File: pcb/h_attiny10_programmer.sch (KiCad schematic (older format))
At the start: 43 parts, among them J1 PWR, J2 AVR-TPI-6, J3 Conn_01x03, J4 Conn_01x03, J5 Conn_01x03, J6 Conn_01x03, J7 Conn_01x03, J8 Conn_01x03, Q1 2N3906, SW1 SW_Push, SW2 SW_Push, SW3 SW_Push, SW4 SW_Push, U1 AM1SS-n(j)z, U2 PC817, U3 L7805, U4 ATtiny10-TS

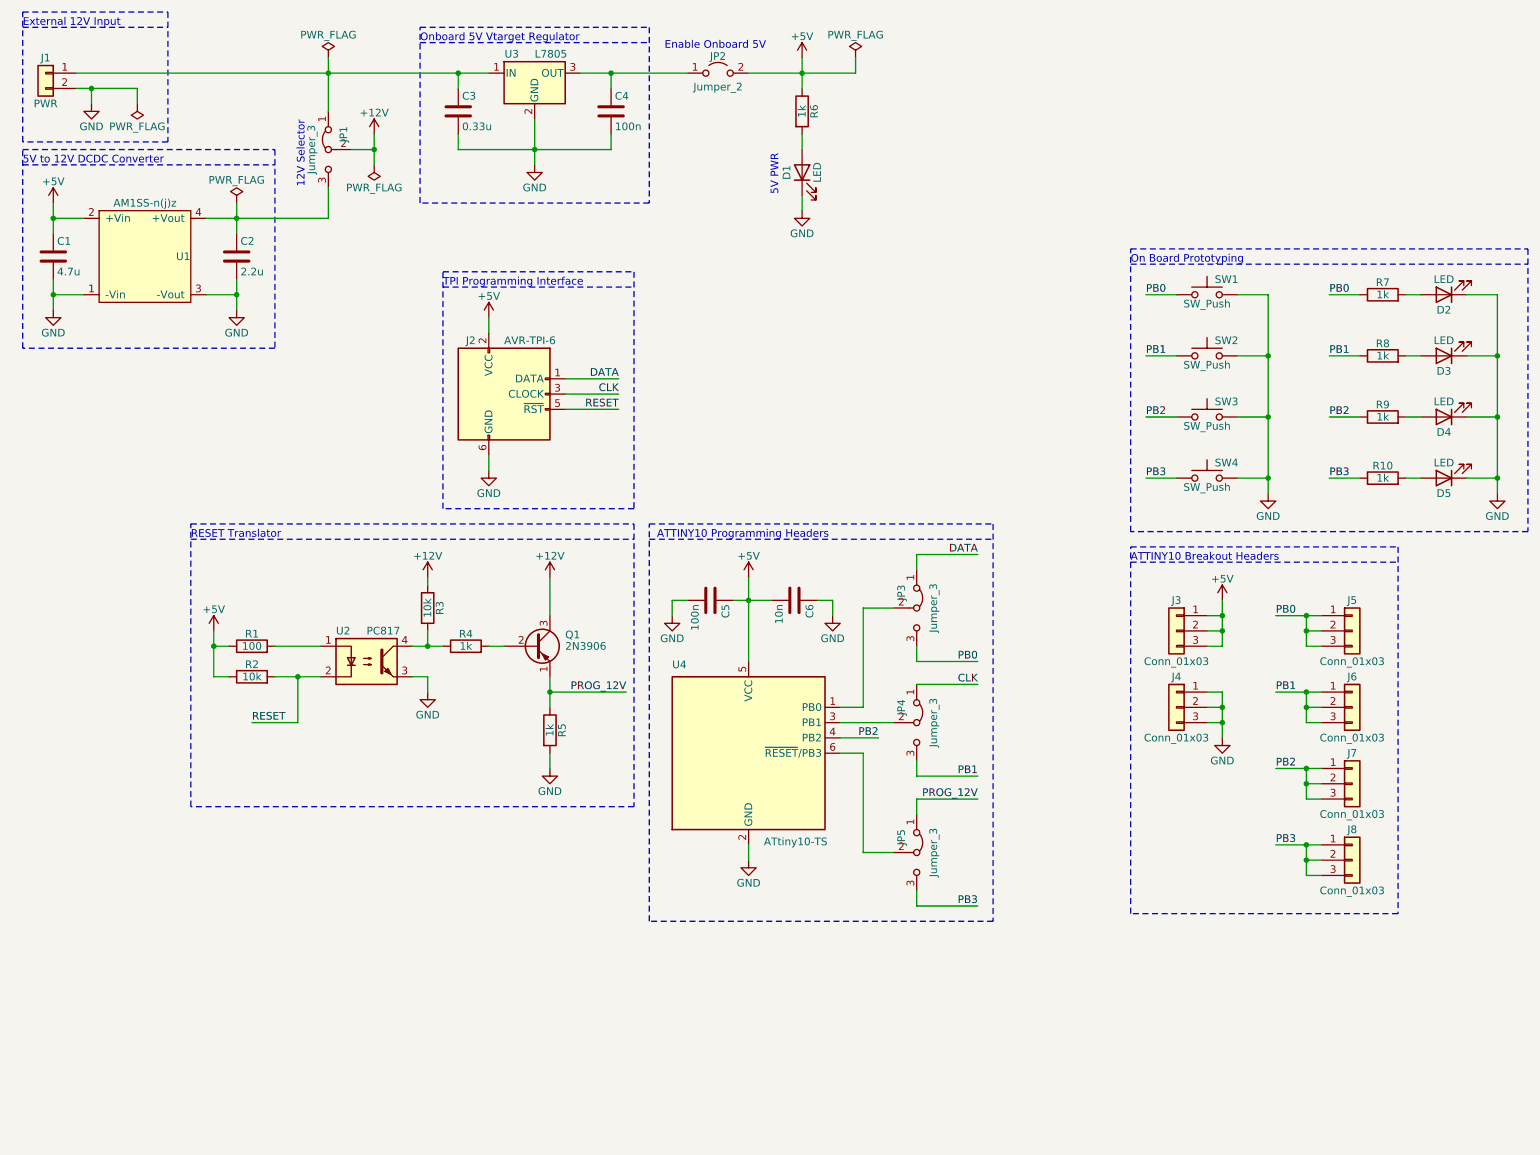
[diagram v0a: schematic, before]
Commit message: change DCDC converter
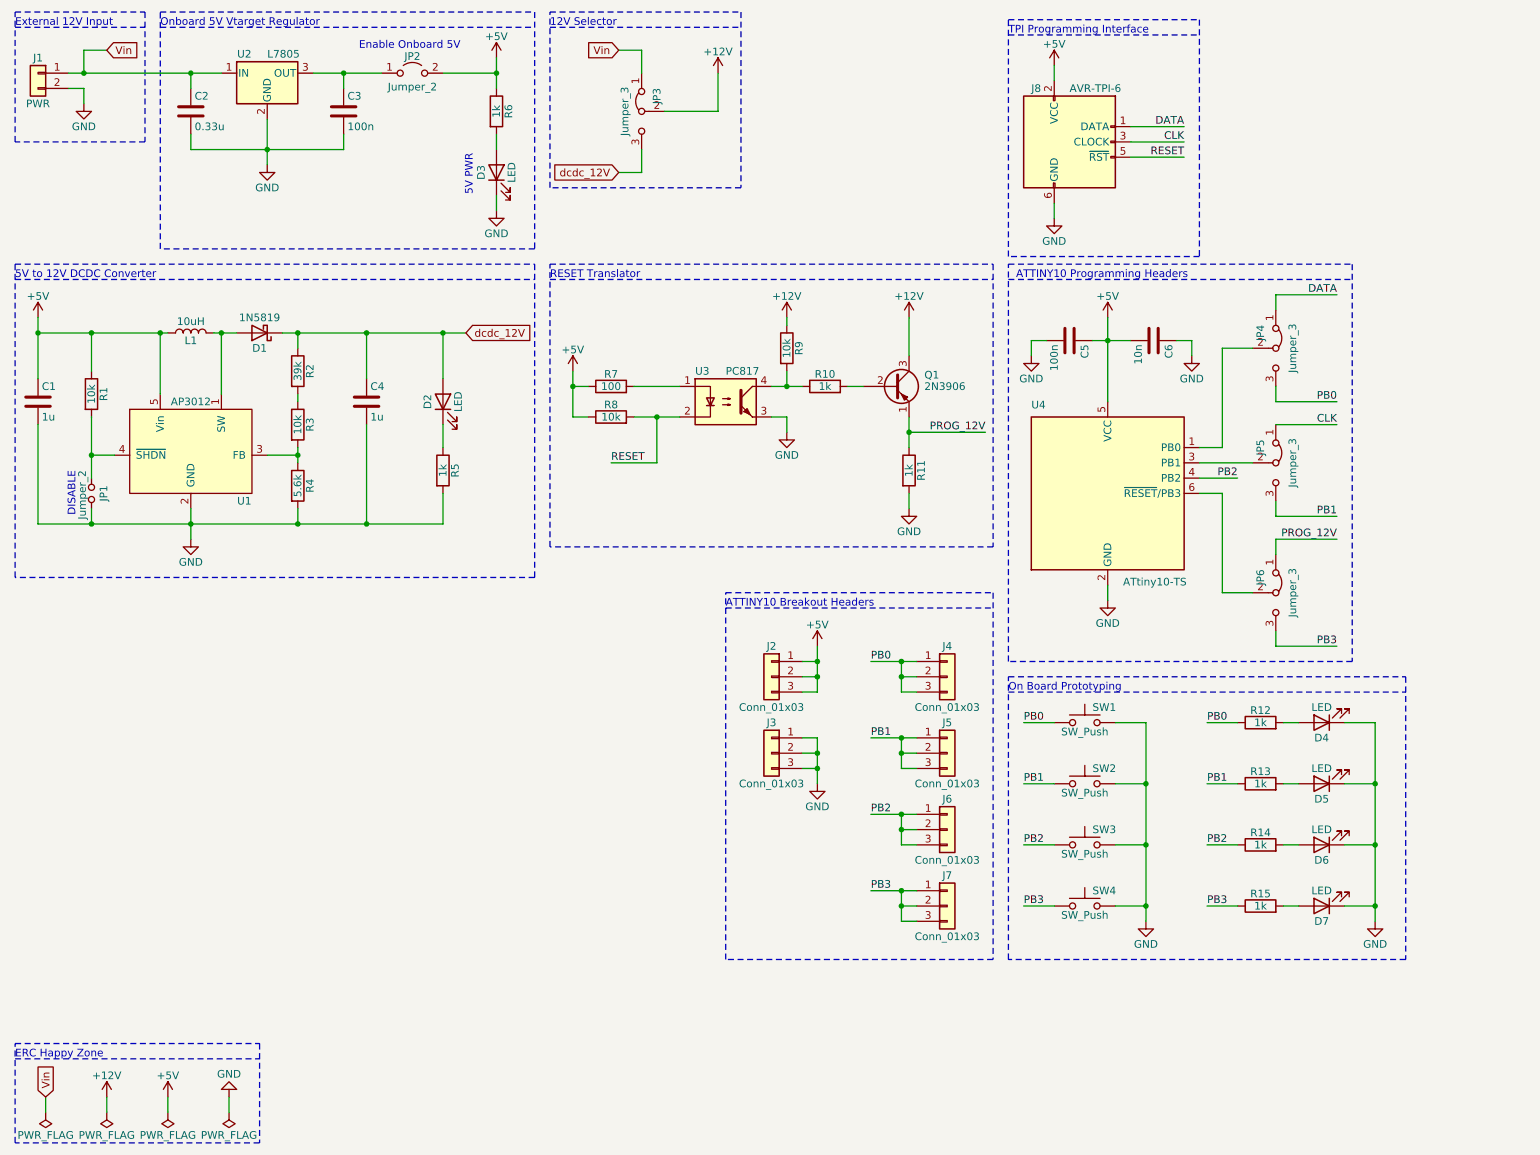
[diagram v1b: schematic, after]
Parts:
- removed U1: AM1SS-n(j)z, Connector_PinHeader_2.54mm:PinHeader_1x04_P2.54mm_Vertical, symbol aimtec_dcdc:AM1SS-n(j)z
- added D1: 1N5819, Diode_THT:D_DO-41_SOD81_P10.16mm_Horizontal, symbol Device:D_Schottky
- added D2: LED, LED_THT:LED_D5.0mm, symbol Device:LED
- added JP1: Jumper_2, Connector_PinHeader_2.54mm:PinHeader_1x02_P2.54mm_Vertical, symbol Device:Jumper_NO_Small
- added L1: 10uH, pl_inductor:sumida_cdrh2d11, symbol Device:L
- added R1, R3: 10k, Resistor_THT:R_Axial_DIN0207_L6.3mm_D2.5mm_P10.16mm_Horizontal, symbol Device:R
- added R2: 39k, Resistor_THT:R_Axial_DIN0207_L6.3mm_D2.5mm_P10.16mm_Horizontal, symbol Device:R
- added R4: 5.6k, Resistor_THT:R_Axial_DIN0207_L6.3mm_D2.5mm_P10.16mm_Horizontal, symbol Device:R
- added R5: 1k, Resistor_THT:R_Axial_DIN0207_L6.3mm_D2.5mm_P10.16mm_Horizontal, symbol Device:R
- added U1: AP3012, Package_TO_SOT_SMD:SOT-23-5, symbol pl_diodesInc_dcdc:AP3012
- C1: value 4.7u -> 1u; footprint Capacitor_THT:CP_Radial_D5.0mm_P2.50mm -> Capacitor_SMD:C_0805_2012Metric_Pad1.18x1.45mm_HandSolder
- C4: renamed from C2; value 2.2u -> 1u; footprint Capacitor_THT:CP_Radial_D5.0mm_P2.50mm -> Capacitor_SMD:C_0805_2012Metric_Pad1.18x1.45mm_HandSolder
- renumbered C3 to C2, C4 to C3, D1 to D3, D2 to D4, D3 to D5, D4 to D6, D5 to D7, J3 to J2, J4 to J3, J5 to J4, J6 to J5, J7 to J6, J8 to J7, J2 to J8, JP1 to JP3, JP3 to JP4, JP4 to JP5, JP5 to JP6, R4 to R10, R5 to R11, R7 to R12, R8 to R13, R9 to R14, R10 to R15, R1 to R7, R2 to R8, R3 to R9, U3 to U2, U2 to U3
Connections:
- net +5V: now also L1.2, R1.1, U1.5 (Vin)
- net GND: now also JP1.2, R4.2, R5.2, U1.2 (GND)
- net dcdc_12V: now reaches C4.1, JP3.3 (B)
- net dcdc_12V: now also D1.1 (K), D2.2 (A), R2.1
- net Vin: now reaches C2.1, J1.1 (Pin_1), JP3.1 (A), U2.1 (IN)
- new net: D1.2 (A), L1.1, U1.1 (SW)
- new net: R3.2, R4.1, U1.3 (FB)
- new net: JP1.1, R1.2, U1.4 (~SHDN)
- new net: R2.2, R3.1
- new net: D2.1 (K), R5.1
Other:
- note added: "DISABLE"
- note added: "ERC Happy Zone"
- moved on the sheet: C1, C2, C3, C4, C5, C6, D3, D4, D5, D6, D7, J1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

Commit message: change ATTINY10 footprint to DIP-6 for breakout
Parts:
- U4: footprint Package_TO_SOT_SMD:SOT-23-6 -> Package_DIP:DIP-6_W7.62mm
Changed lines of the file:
@@
 F 0 "U4" H 7200 4250 50  0000 L BNN
 F 1 "ATtiny10-TS" H 7800 3150 50  0000 L TNN
-F 2 "Package_TO_SOT_SMD:SOT-23-6" H 7700 3700 50  0001 C CIN
+F 2 "Package_DIP:DIP-6_W7.62mm" H 7700 3700 50  0001 C CIN
 F 3 "http://ww1.microchip.com/downloads/en/DeviceDoc/Atmel-8127-AVR-8-bit-Microcontroller-ATtiny4-ATtiny5-ATtiny9-ATtiny10_Datasheet.pdf" H 7700 3700 50  0001 C CNN
 	1    7700 3700

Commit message: vin change to terminal block
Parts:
- added H1, H2, H3, H4: M3, MountingHole:MountingHole_3.5mm, symbol Mechanical:MountingHole
- added JP10, JP7, JP8, JP9: Jumper, Connector_PinHeader_2.54mm:PinHeader_1x02_P2.54mm_Vertical, symbol Device:Jumper_NO_Small
- J1: footprint Connector_PinHeader_2.54mm:PinHeader_1x02_P2.54mm_Vertical -> TerminalBlock:TerminalBlock_bornier-2_P5.08mm
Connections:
- net PB0: now also JP7.1; no longer R12.1
- net PB1: now also JP8.1; no longer R13.1
- net PB2: now also JP9.1; no longer R14.1
- net PB3: now also JP10.1; no longer R15.1
- new net: JP7.2, R12.1
- new net: JP8.2, R13.1
- new net: JP9.2, R14.1
- new net: JP10.2, R15.1
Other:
- moved on the sheet: C5, C6, D4, D5, D6, D7, J2, J3, J4, J5, J6, J7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

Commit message: change attiny10 capacitor footprint to smd
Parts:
- C5, C6: footprint Capacitor_THT:C_Disc_D4.3mm_W1.9mm_P5.00mm -> Capacitor_SMD:C_0805_2012Metric_Pad1.18x1.45mm_HandSolder
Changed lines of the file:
@@
 F 0 "C6" H 7975 2800 50  0000 L CNN
 F 1 "10n" H 7975 2600 50  0000 L CNN
-F 2 "Capacitor_THT:C_Disc_D4.3mm_W1.9mm_P5.00mm" H 7988 2550 50  0001 C CNN
+F 2 "Capacitor_SMD:C_0805_2012Metric_Pad1.18x1.45mm_HandSolder" H 7988 2550 50  0001 C CNN
 F 3 "~" H 7950 2700 50  0001 C CNN
 	1    7950 2700
@@
 F 0 "C5" H 7425 2800 50  0000 L CNN
 F 1 "100n" H 7425 2600 50  0000 L CNN
-F 2 "Capacitor_THT:C_Disc_D4.3mm_W1.9mm_P5.00mm" H 7438 2550 50  0001 C CNN
+F 2 "Capacitor_SMD:C_0805_2012Metric_Pad1.18x1.45mm_HandSolder" H 7438 2550 50  0001 C CNN
 F 3 "~" H 7400 2700 50  0001 C CNN
 	1    7400 2700

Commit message: PNP incorrect orientaiton, mirrored along x axis in schematic to fix
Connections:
- net +12V: now also Q1.1 (E); no longer Q1.3 (C)
- net PROG_12V: now also Q1.3 (C); no longer Q1.1 (E)
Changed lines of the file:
@@
 F 3 "https://www.onsemi.com/pub/Collateral/2N3906-D.PDF" H 6300 3000 50  0001 L CNN
 	1    6300 3000
-	1    0    0    -1
+	1    0    0    1
 $EndComp
 Wire Wire Line

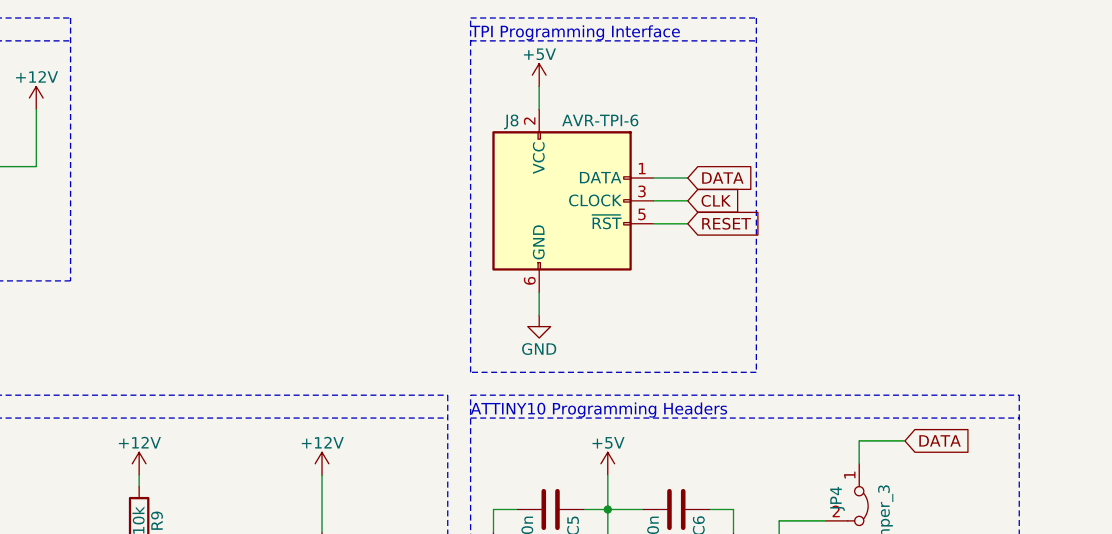
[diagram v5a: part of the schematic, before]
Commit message: connect TPIDATA to MISO and MOSI
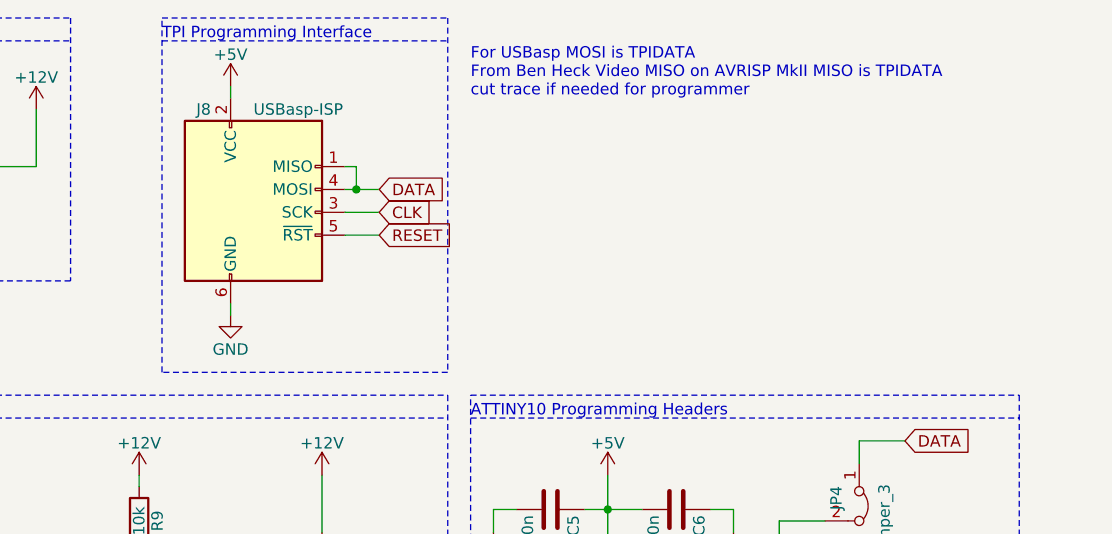
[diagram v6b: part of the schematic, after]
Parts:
- removed J8: AVR-TPI-6, Connector_PinHeader_2.54mm:PinHeader_2x03_P2.54mm_Vertical, symbol Connector:AVR-TPI-6
- added J8: USBasp-ISP, Connector_PinHeader_2.54mm:PinHeader_2x03_P2.54mm_Vertical, symbol Connector:AVR-ISP-6
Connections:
- net +5V: now also J8.2 (VCC)
- net CLK: now also J8.3 (SCK)
- net DATA: now also J8.1 (MISO), J8.4 (MOSI)
- net GND: now also J8.6 (GND)
- net RESET: now also J8.5 (~RST)
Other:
- note added: "For USBasp MOSI is TPIDATA\nFrom Ben Heck Video MISO on AVRISP MkII MISO is TPIDATA\ncut trace if needed for programmer"
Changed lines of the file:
@@
 $EndComp
 Wire Wire Line
-	7850 1250 8000 1250
-Wire Wire Line
-	7850 1350 8000 1350
-Wire Wire Line
-	8000 1450 7850 1450
-Wire Notes Line
-	8300 550  8300 2100
-Wire Notes Line
-	7050 550  8300 550
-Wire Notes Line
-	7050 2100 7050 550
-Wire Notes Line
-	8300 2100 7050 2100
-Wire Notes Line
-	7050 650  8300 650
-Text Notes 7050 650  0    50   ~ 0
+	6500 1300 6550 1300
+Wire Wire Line
+	6500 1400 6650 1400
+Wire Wire Line
+	6650 1500 6500 1500
+Wire Notes Line
+	6950 550  6950 2100
+Wire Notes Line
+	5700 550  6950 550
+Wire Notes Line
+	5700 2100 5700 550
+Wire Notes Line
+	6950 2100 5700 2100
+Wire Notes Line
+	5700 650  6950 650
+Text Notes 5700 650  0    50   ~ 0
 TPI Programming Interface
 Wire Wire Line
@@
 $EndComp
 $Comp
-L Connector:AVR-TPI-6 J8
-U 1 1 5FDF9B9A
-P 7450 1350
-F 0 "J8" H 7200 1700 50  0000 L CNN
-F 1 "AVR-TPI-6" H 7450 1700 50  0000 L CNN
-F 2 "Connector_PinHeader_2.54mm:PinHeader_2x03_P2.54mm_Vertical" V 7200 1300 50  0001 C CNN
-F 3 " ~" H 6175 800 50  0001 C CNN
-	1    7450 1350
-	1    0    0    -1
-$EndComp
-Wire Wire Line
-	7350 1850 7350 1750
-$Comp
 L power:GND #PWR017
 U 1 1 5FDF651F
-P 7350 1850
-F 0 "#PWR017" H 7350 1600 50  0001 C CNN
-F 1 "GND" H 7350 1700 50  0000 C CNN
-F 2 "" H 7350 1850 50  0001 C CNN
-F 3 "" H 7350 1850 50  0001 C CNN
-	1    7350 1850
-	1    0    0    -1
-$EndComp
-Wire Wire Line
-	7350 950  7350 850
+P 6000 1850
+F 0 "#PWR017" H 6000 1600 50  0001 C CNN
+F 1 "GND" H 6000 1700 50  0000 C CNN
+F 2 "" H 6000 1850 50  0001 C CNN
+F 3 "" H 6000 1850 50  0001 C CNN
+	1    6000 1850
+	1    0    0    -1
+$EndComp
 $Comp
 L power:+5V #PWR016
 U 1 1 5FDF54B6
-P 7350 850
-F 0 "#PWR016" H 7350 700 50  0001 C CNN
-F 1 "+5V" H 7350 990 50  0000 C CNN
-F 2 "" H 7350 850 50  0001 C CNN
-F 3 "" H 7350 850 50  0001 C CNN
-	1    7350 850
+P 6000 850
+F 0 "#PWR016" H 6000 700 50  0001 C CNN
+F 1 "+5V" H 6000 990 50  0000 C CNN
+F 2 "" H 6000 850 50  0001 C CNN
+F 3 "" H 6000 850 50  0001 C CNN
+	1    6000 850
 	1    0    0    -1
 $EndComp
@@
 Text GLabel 8950 4050 2    50   Input ~ 0
 PB2
-Text GLabel 8000 1250 2    50   Input ~ 0
+Text GLabel 6650 1300 2    50   Input ~ 0
 DATA
-Text GLabel 8000 1350 2    50   Input ~ 0
+Text GLabel 6650 1400 2    50   Input ~ 0
 CLK
-Text GLabel 8000 1450 2    50   Input ~ 0
+Text GLabel 6650 1500 2    50   Input ~ 0
 RESET
 Text GLabel 6500 3300 2    50   Input ~ 0
@@
 	1    0    0    -1
 $EndComp
+$Comp
+L Connector:AVR-ISP-6 J8
+U 1 1 5FDEE36F
+P 6100 1400
+F 0 "J8" H 5850 1850 50  0000 L CNN
+F 1 "USBasp-ISP" H 6100 1850 50  0000 L CNN
+F 2 "Connector_PinHeader_2.54mm:PinHeader_2x03_P2.54mm_Vertical" V 5850 1450 50  0001 C CNN
+F 3 " ~" H 4825 850 50  0001 C CNN
+	1    6100 1400
+	1    0    0    -1
+$EndComp
+Wire Wire Line
+	6000 900  6000 850
+Wire Wire Line
+	6000 1800 6000 1850
+Wire Wire Line
+	6500 1200 6550 1200
+Wire Wire Line
+	6550 1200 6550 1300
+Connection ~ 6550 1300
+Wire Wire Line
+	6550 1300 6650 1300
+Text Notes 7050 900  0    50   ~ 0
+For USBasp MOSI is TPIDATA\nFrom Ben Heck Video MISO on AVRISP MkII MISO is TPIDATA\ncut trace if needed for programmer
 $EndSCHEMATC
